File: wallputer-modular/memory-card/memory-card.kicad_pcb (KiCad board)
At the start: 2 copper layers, 99.7 x 99.7 mm, 8 parts, among them U1 HM62256BLP, U2 74HC00, U3 SST39SF010

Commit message: add activation indicators
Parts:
- added D1: Blue, LED_SMD:LED_1206_3216Metric, F.Cu at (154.8, 140.3)
- added D2: Blue, LED_SMD:LED_1206_3216Metric, F.Cu at (74.8, 139.1)
- added Q1: BSS84, Package_TO_SOT_SMD:SOT-23, F.Cu at (146.7, 140.0)
- added Q2: BSS84, Package_TO_SOT_SMD:SOT-23, F.Cu at (82.9, 139.4)
- added R2: 680, Resistor_SMD:R_0603_1608Metric, F.Cu at (150.5, 140.3)
- added R3: 5.1k, Resistor_SMD:R_0603_1608Metric, F.Cu at (142.7, 139.1)
- added R4: 100k, Resistor_SMD:R_0603_1608Metric, F.Cu at (142.7, 141.0)
- added R5: 5.1k, Resistor_SMD:R_0603_1608Metric, F.Cu at (86.8, 140.3)
- added R6: 100k, Resistor_SMD:R_0603_1608Metric, F.Cu at (86.8, 138.4)
- added R7: 680, Resistor_SMD:R_0603_1608Metric, F.Cu at (78.9, 139.1)
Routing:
- net +5V: track 187.0 -> 274.5 mm, vias 3 -> 7
- net ROM/: track 184.9 -> 202.9 mm, vias 3 -> 5
- net RAM/: track 161.3 -> 177.6 mm, vias 2 -> 4
- net GND: track 3.59 -> 17.8 mm
- net Net-(Q1-G): track 0.00 -> 4.83 mm
- net Net-(Q2-G): track 0.00 -> 4.75 mm
- net Net-(D1-A): track 0.00 -> 2.99 mm
- net Net-(Q2-D): track 0.00 -> 2.32 mm
- net Net-(Q1-D): track 0.00 -> 2.17 mm
- net Net-(D2-A): track 0.00 -> 1.91 mm

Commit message: shift down a bit, and make it upside down
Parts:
- moved C2 8.40 mm to (158.7, 108.7)
- moved D1 8.40 mm to (154.8, 148.7)
- moved D2 8.40 mm to (74.8, 147.5)
- moved Q1 8.40 mm to (146.7, 148.4)
- moved Q2 8.40 mm to (82.9, 147.8)
- moved R1 8.40 mm to (85.7, 108.7)
- moved R2 8.40 mm to (150.5, 148.7)
- moved R3 8.40 mm to (142.7, 147.5)
- moved R4 8.40 mm to (142.7, 149.4)
- moved R5 8.40 mm to (86.8, 148.7)
- moved R6 8.40 mm to (86.8, 146.8)
- moved R7 8.40 mm to (78.9, 147.5)
- moved U1 8.40 mm to (151.1, 112.5)
- moved U2 8.40 mm to (151.1, 87.1)
- moved C1 8.40 mm to (82.5, 102.4)
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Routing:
- net /A13: track 117.3 -> 125.8 mm
- net /A11: track 124.9 -> 133.4 mm
- net /A15: track 70.0 -> 78.5 mm
- net /A7: track 126.2 -> 134.7 mm
- net /A6: track 128.7 -> 137.2 mm
- net /A12: track 123.7 -> 132.1 mm
- net /A0: track 144.0 -> 152.5 mm
- net RAM/: track 177.6 -> 186.0 mm
- net /D0: track 143.5 -> 151.9 mm
- net /A1: track 141.5 -> 149.9 mm
- net RW/: track 119.9 -> 128.3 mm
- net /A9: track 122.5 -> 130.9 mm
- net ROM_PGM/: track 61.7 -> 70.1 mm
- net ACC/: track 87.6 -> 96.0 mm
- net /D7: track 132.1 -> 140.5 mm
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
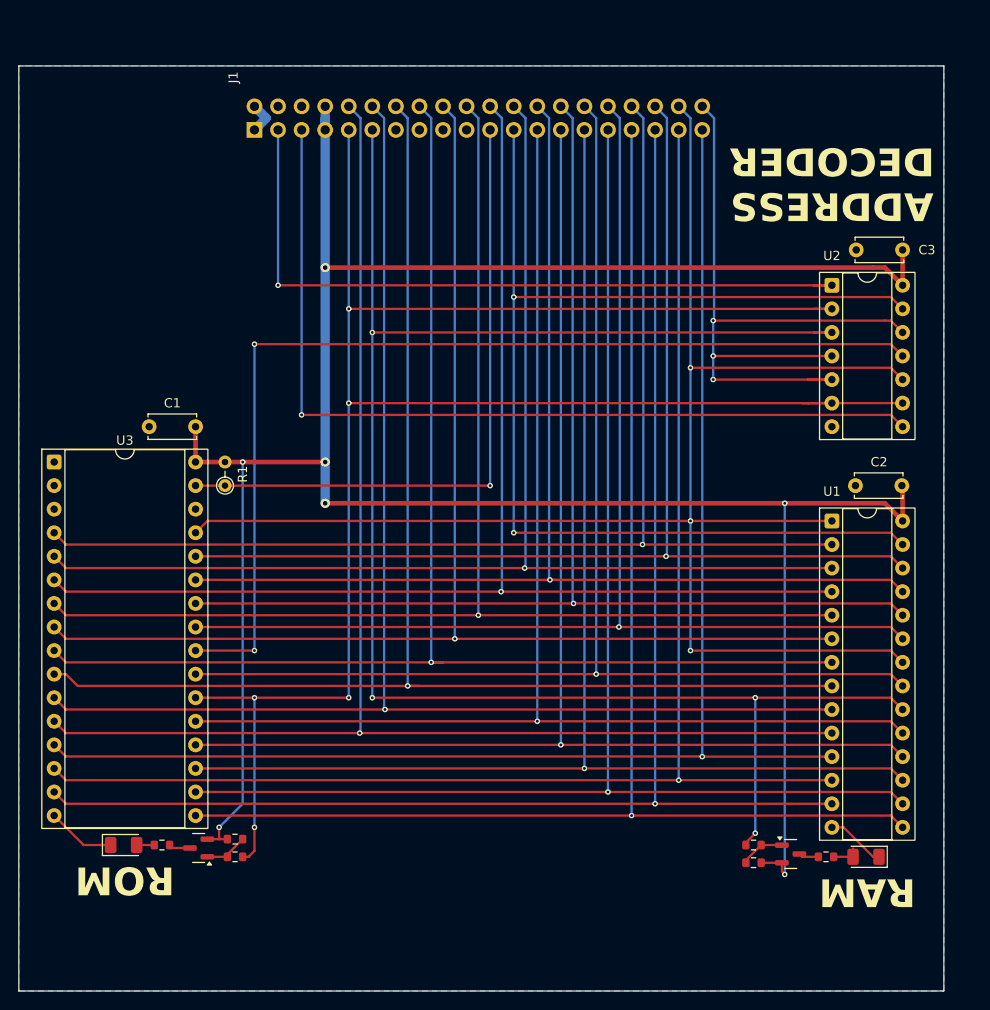
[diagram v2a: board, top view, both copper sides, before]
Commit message: add card name
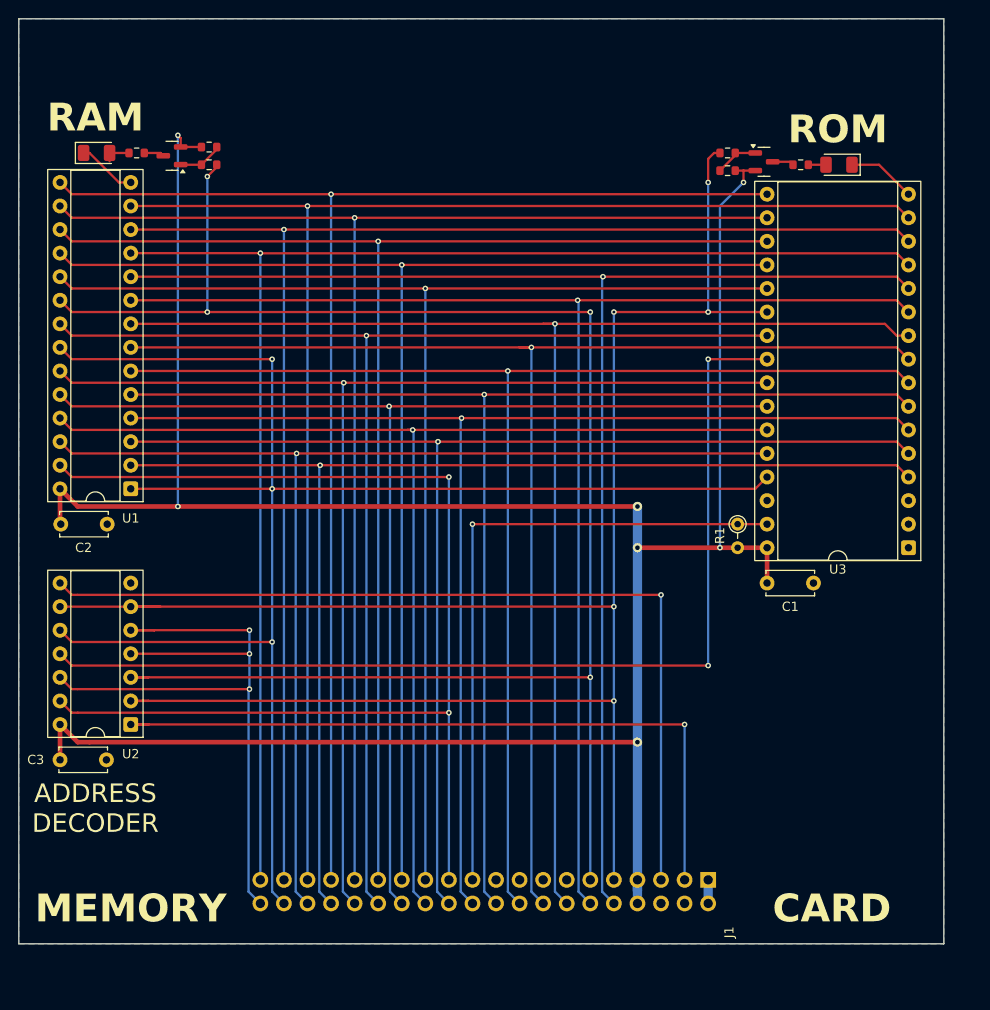
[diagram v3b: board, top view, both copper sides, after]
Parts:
- moved D1 112.4 mm to (71.9, 72.9), turned to 0 degrees
- moved D2 106.4 mm to (151.9, 74.2), turned to 180 degrees
- moved R2 106.2 mm to (76.2, 72.9), turned to 0 degrees
- moved C3 106.1 mm to (67.9, 138.3), turned to 0 degrees
- moved R7 100.6 mm to (147.8, 74.2), turned to 180 degrees
- moved Q1 100.5 mm to (80.0, 73.2), turned to 180 degrees
- moved R4 96.9 mm to (84.0, 72.2), turned to 180 degrees
- moved Q2 95.8 mm to (143.8, 73.8), turned to 0 degrees
- moved J1 94.5 mm to (137.8, 151.2), turned to -90 degrees
- moved R3 93.9 mm to (84.0, 74.2), turned to 0 degrees
- moved R5 92.6 mm to (139.9, 72.9), turned to 180 degrees
- moved U3 92.5 mm to (159.4, 115.4), turned to 180 degrees
- moved C2 90.7 mm to (68.0, 112.9), turned to 0 degrees
- moved R6 89.5 mm to (139.9, 74.8), turned to 0 degrees
- moved U2 89.2 mm to (75.6, 134.5), turned to 180 degrees
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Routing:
- net GND: track 17.8 -> 16.8 mm
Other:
- board text added: "CARD"
- board text added: "MEMORY"
